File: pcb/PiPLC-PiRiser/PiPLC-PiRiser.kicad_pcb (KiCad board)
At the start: 2 copper layers, 51.9 x 29.4 mm, 2 parts, among them J1 Male, J2 Female

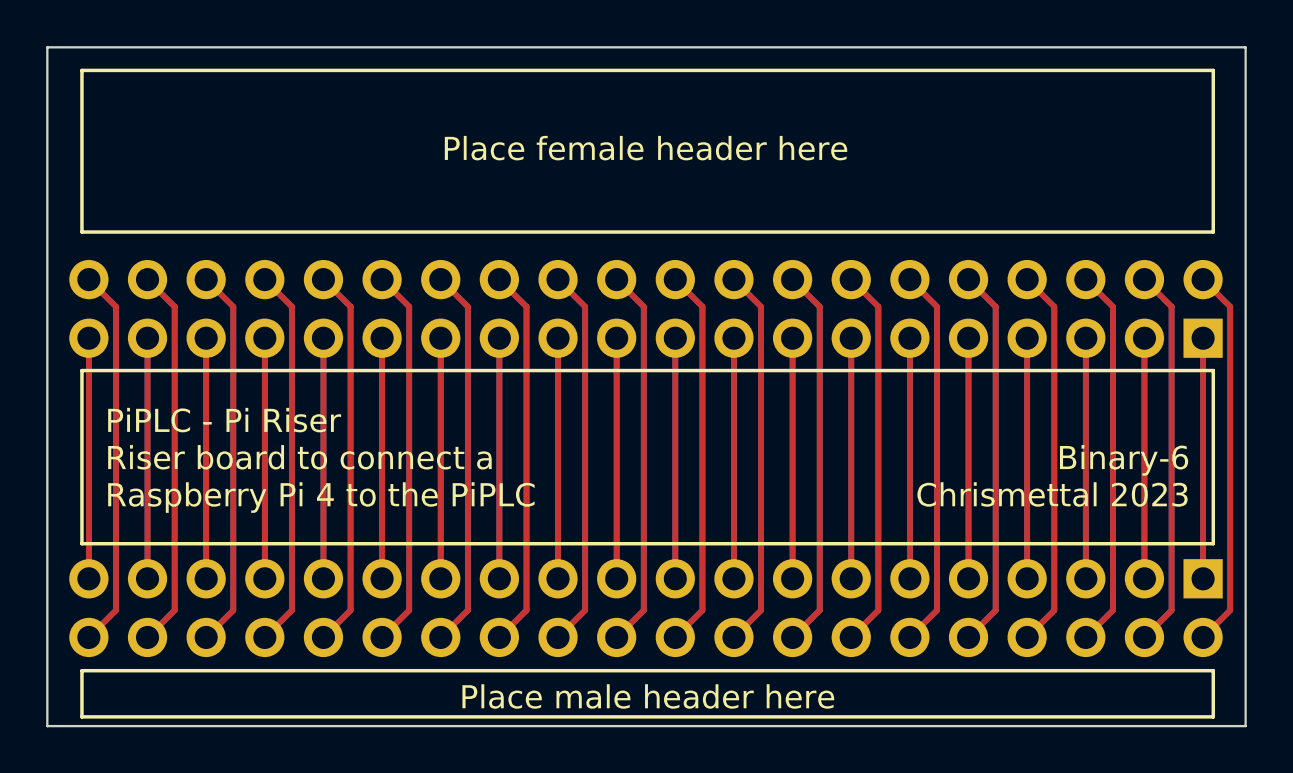
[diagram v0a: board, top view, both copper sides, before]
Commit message: [PiRiser] Remove bad manual from silkscreen
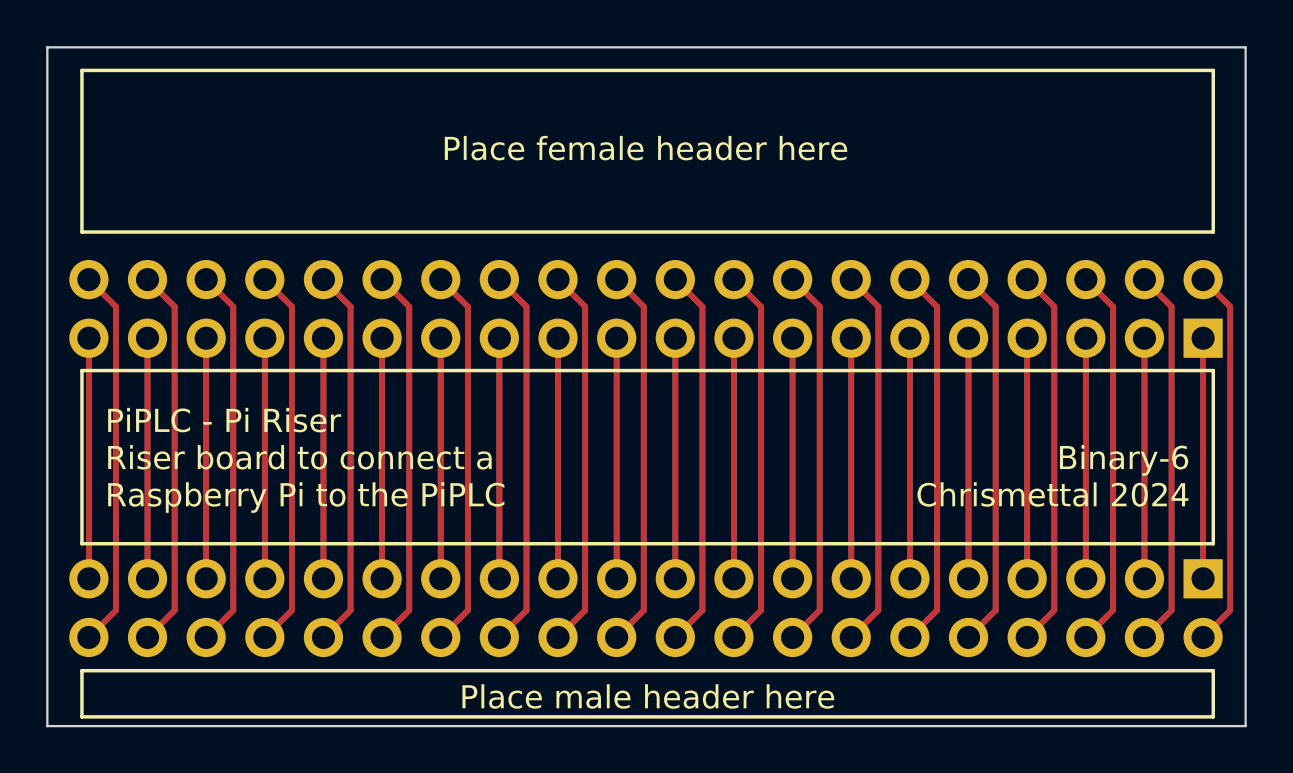
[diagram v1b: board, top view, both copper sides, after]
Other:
- board text added: "Binary-6 Chrismettal 2024"
- board text added: "PiPLC - Pi Riser Riser board to connect a Raspberry Pi to the PiPLC"
- board text removed: "Binary-6 Chrismettal 2023"
- board text removed: "PiPLC - Pi Riser Riser board to connect a Raspberry Pi 4 to the PiPLC"
- board text removed: "This side needs to face inward of the PLC"
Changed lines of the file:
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@@
   (gr_rect (start 107.2 85.4) (end 159.1 114.8)
     (stroke (width 0.1) (type default)) (fill none) (layer "Edge.Cuts"))
-  (gr_text "This side needs to face inward of the PLC" (at 133.2 103.4) (layer "B.SilkS")
-    (effects (font (size 1 1) (thickness 0.15)) (justify bottom mirror))
-  )
-  (gr_text "Binary-6\nChrismettal 2023" (at 156.7 105.4) (layer "F.SilkS")
+  (gr_text "Binary-6\nChrismettal 2024" (at 156.7 105.4) (layer "F.SilkS")
     (effects (font (size 1 1) (thickness 0.15)) (justify right bottom))
   )
-  (gr_text "PiPLC - Pi Riser\nRiser board to connect a\nRaspberry Pi 4 to the PiPLC" (at 109.7 105.4) (layer "F.SilkS")
+  (gr_text "PiPLC - Pi Riser\nRiser board to connect a\nRaspberry Pi to the PiPLC" (at 109.7 105.4) (layer "F.SilkS")
     (effects (font (size 1 1) (thickness 0.15)) (justify left bottom))
   )
